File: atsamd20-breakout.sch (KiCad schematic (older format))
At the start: 37 parts, among them J1 SWD, J2 Left, J3 Right, Q1 BC847BS, SW1 SW_Push, U1 ATSAMD20E18A-A, Y1 32.768kHz, Y2 8MHz

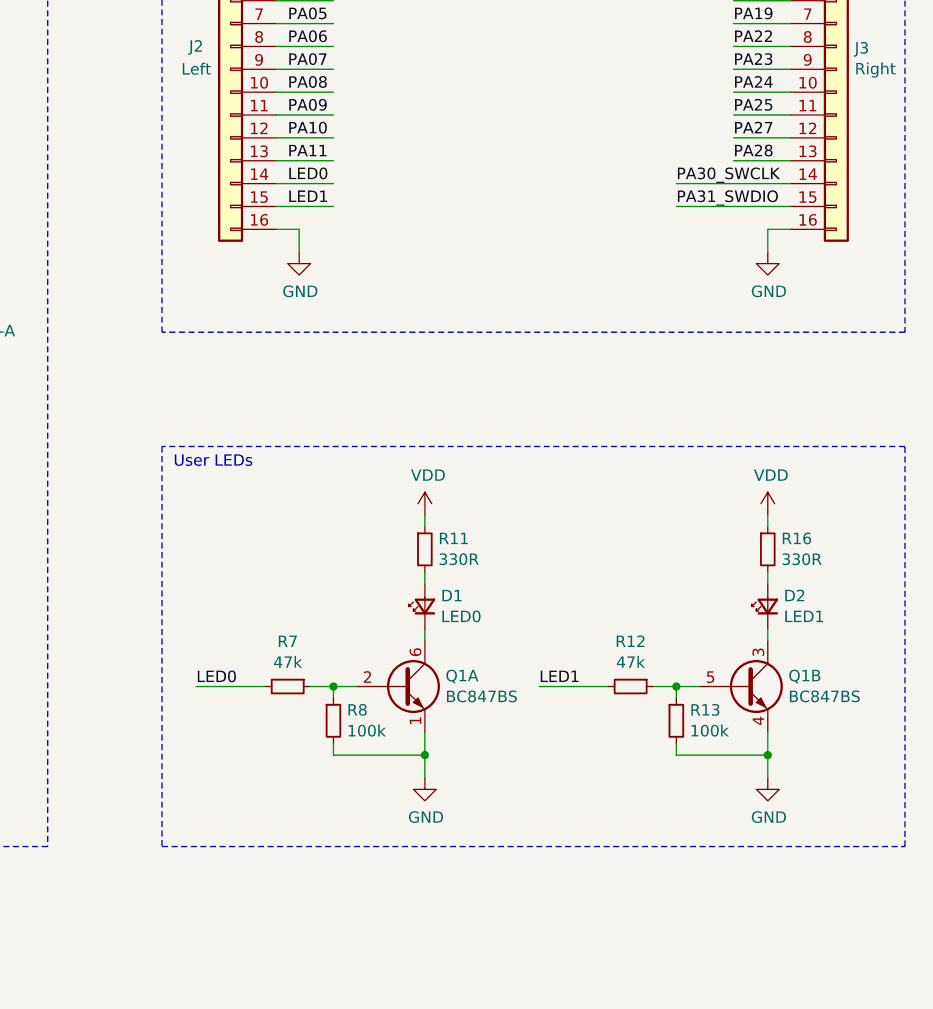
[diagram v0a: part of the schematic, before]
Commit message: Replaced LED1 pin with RESET, removed LED1 circuit
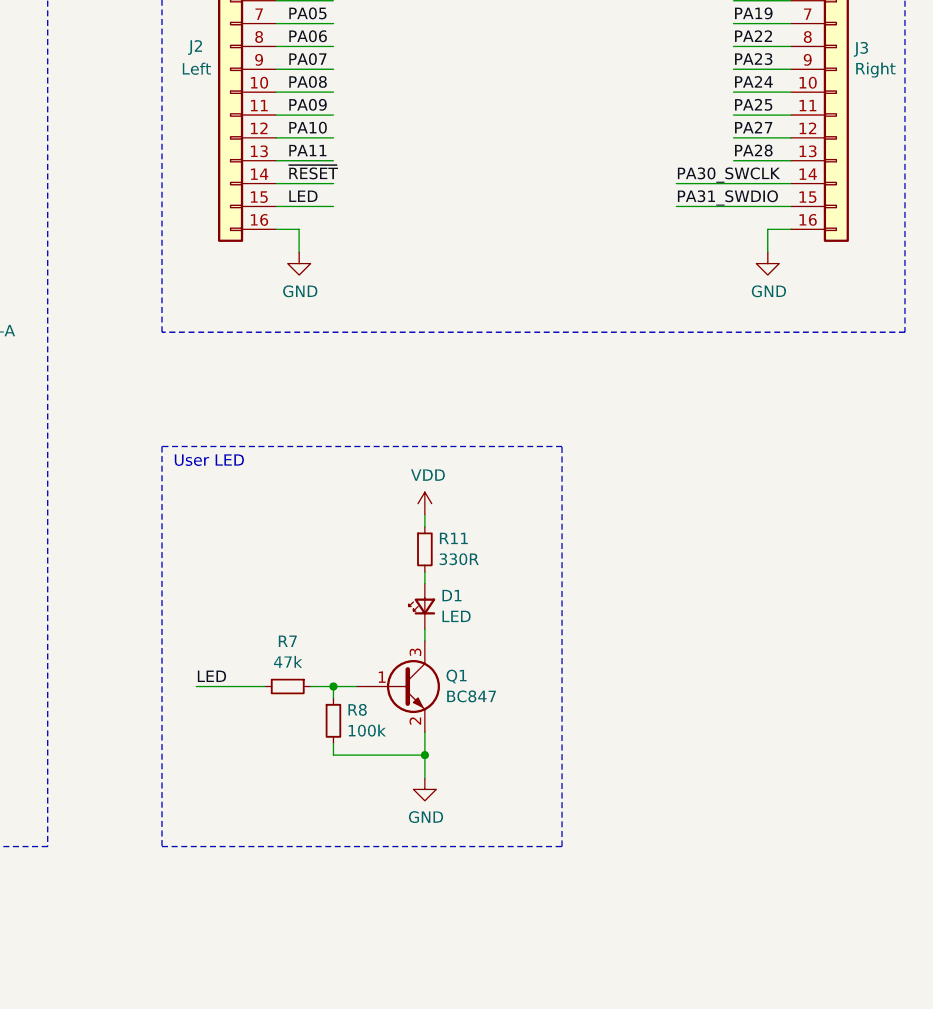
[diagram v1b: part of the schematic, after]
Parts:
- removed D2: LED1, LED_SMD:LED_0805_2012Metric, symbol Device:LED_Small
- removed Q1: BC847BS, Package_TO_SOT_SMD:SOT-363_SC-70-6, symbol Transistor_BJT:BC847BS
- removed R12: 47k, Resistor_SMD:R_0603_1608Metric, symbol Device:R_Small
- removed R13: 100k, Resistor_SMD:R_0603_1608Metric, symbol Device:R_Small
- removed R16: 330R, Resistor_SMD:R_0603_1608Metric, symbol Device:R_Small
- added Q1: BC847, Package_TO_SOT_SMD:SOT-23, symbol Transistor_BJT:BC847
- D1: value LED0 -> LED
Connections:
- net labels added: LED
- net labels removed: LED0, LED1
- wire segments 156 -> 145
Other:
- note added: "User LED"
- note removed: "User LEDs"
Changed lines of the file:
@@
 Wire Wire Line
 	9750 2950 10250 2950
-Text Label 8050 2850 0    50   ~ 0
-LED0
 Text Label 8050 2950 0    50   ~ 0
-LED1
+LED
 $Comp
 L Device:R_Small R9
@@
 Board I/O headers
 $Comp
-L Transistor_BJT:BC847BS Q1
-U 1 1 5F4F8DAD
-P 8550 5050
-F 0 "Q1" H 8740 5096 50  0000 L CNN
-F 1 "BC847BS" H 8740 5005 50  0000 L CNN
-F 2 "Package_TO_SOT_SMD:SOT-363_SC-70-6" H 8750 5150 50  0001 C CNN
-F 3 "https://assets.nexperia.com/documents/data-sheet/BC847BS.pdf" H 8550 5050 50  0001 C CNN
-	1    8550 5050
-	1    0    0    -1
-$EndComp
-$Comp
-L Transistor_BJT:BC847BS Q1
-U 2 1 5F4F9E18
-P 10050 5050
-F 0 "Q1" H 10240 5096 50  0000 L CNN
-F 1 "BC847BS" H 10240 5005 50  0000 L CNN
-F 2 "Package_TO_SOT_SMD:SOT-363_SC-70-6" H 10250 5150 50  0001 C CNN
-F 3 "https://assets.nexperia.com/documents/data-sheet/BC847BS.pdf" H 10050 5050 50  0001 C CNN
-	2    10050 5050
-	1    0    0    -1
-$EndComp
-$Comp
 L Device:LED_Small D1
 U 1 1 5F517E2A
 P 8650 4700
 F 0 "D1" V 8696 4630 50  0000 R CNN
-F 1 "LED0" V 8605 4630 50  0000 R CNN
+F 1 "LED" V 8605 4630 50  0000 R CNN
 F 2 "LED_SMD:LED_0805_2012Metric" V 8650 4700 50  0001 C CNN
 F 3 "~" V 8650 4700 50  0001 C CNN
 	1    8650 4700
-	0    -1   -1   0
-$EndComp
-$Comp
-L Device:LED_Small D2
-U 1 1 5F518B36
-P 10150 4700
-F 0 "D2" V 10196 4630 50  0000 R CNN
-F 1 "LED1" V 10105 4630 50  0000 R CNN
-F 2 "LED_SMD:LED_0805_2012Metric" V 10150 4700 50  0001 C CNN
-F 3 "~" V 10150 4700 50  0001 C CNN
-	1    10150 4700
 	0    -1   -1   0
 $EndComp
@@
 $EndComp
 $Comp
-L Device:R_Small R16
-U 1 1 5F519929
-P 10150 4450
-F 0 "R16" H 10209 4496 50  0000 L CNN
-F 1 "330R" H 10209 4405 50  0000 L CNN
-F 2 "Resistor_SMD:R_0603_1608Metric" H 10150 4450 50  0001 C CNN
-F 3 "~" H 10150 4450 50  0001 C CNN
-	1    10150 4450
-	1    0    0    -1
-$EndComp
-$Comp
 L Device:R_Small R8
 U 1 1 5F519CFF
@@
 $EndComp
 $Comp
-L Device:R_Small R13
-U 1 1 5F51A312
-P 9750 5200
-F 0 "R13" H 9809 5246 50  0000 L CNN
-F 1 "100k" H 9809 5155 50  0000 L CNN
-F 2 "Resistor_SMD:R_0603_1608Metric" H 9750 5200 50  0001 C CNN
-F 3 "~" H 9750 5200 50  0001 C CNN
-	1    9750 5200
-	1    0    0    -1
-$EndComp
-$Comp
 L Device:R_Small R7
 U 1 1 5F51A9DD
@@
 F 3 "~" H 8050 5050 50  0001 C CNN
 	1    8050 5050
-	0    1    1    0
-$EndComp
-$Comp
-L Device:R_Small R12
-U 1 1 5F51B00D
-P 9550 5050
-F 0 "R12" V 9354 5050 50  0000 C CNN
-F 1 "47k" V 9445 5050 50  0000 C CNN
-F 2 "Resistor_SMD:R_0603_1608Metric" H 9550 5050 50  0001 C CNN
-F 3 "~" H 9550 5050 50  0001 C CNN
-	1    9550 5050
 	0    1    1    0
 $EndComp
@@
 	8250 5050 8350 5050
 Wire Wire Line
-	9650 5050 9750 5050
-Wire Wire Line
-	9750 5050 9750 5100
-Connection ~ 9750 5050
-Wire Wire Line
-	9750 5050 9850 5050
-Wire Wire Line
-	9450 5050 9150 5050
-Wire Wire Line
 	7650 5050 7950 5050
 Text Label 7650 5050 0    50   ~ 0
-LED0
-Text Label 9150 5050 0    50   ~ 0
-LED1
+LED
 $Comp
 L power:GND #PWR024
@@
 	8650 5350 8650 5450
 $Comp
-L power:GND #PWR028
-U 1 1 5F56B570
-P 10150 5450
-F 0 "#PWR028" H 10150 5200 50  0001 C CNN
-F 1 "GND" H 10155 5277 50  0000 C CNN
-F 2 "" H 10150 5450 50  0001 C CNN
-F 3 "" H 10150 5450 50  0001 C CNN
-	1    10150 5450
-	1    0    0    -1
-$EndComp
-Wire Wire Line
-	10150 5250 10150 5350
-Wire Wire Line
-	9750 5300 9750 5350
-Wire Wire Line
-	9750 5350 10150 5350
-Connection ~ 10150 5350
-Wire Wire Line
-	10150 5350 10150 5450
-Wire Wire Line
-	10150 4550 10150 4600
-Wire Wire Line
-	10150 4800 10150 4850
-$Comp
 L power:VDD #PWR023
 U 1 1 5F586EB9
@@
 Wire Wire Line
 	8650 4300 8650 4350
-$Comp
-L power:VDD #PWR027
-U 1 1 5F58EA56
-P 10150 4300
-F 0 "#PWR027" H 10150 4150 50  0001 C CNN
-F 1 "VDD" H 10165 4473 50  0000 C CNN
-F 2 "" H 10150 4300 50  0001 C CNN
-F 3 "" H 10150 4300 50  0001 C CNN
-	1    10150 4300
-	1    0    0    -1
-$EndComp
-Wire Wire Line
-	10150 4300 10150 4350
 Wire Notes Line
-	7500 5750 10750 5750
+	7500 5750 9250 5750
 Wire Notes Line
-	10750 5750 10750 4000
+	9250 5750 9250 4000
 Wire Notes Line
-	10750 4000 7500 4000
+	9250 4000 7500 4000
 Wire Notes Line
 	7500 4000 7500 5750
 Text Notes 7550 4100 0    50   ~ 0
-User LEDs
+User LED
+$Comp
+L Transistor_BJT:BC847 Q1
+U 1 1 5F29391D
+P 8550 5050
+F 0 "Q1" H 8741 5096 50  0000 L CNN
+F 1 "BC847" H 8741 5005 50  0000 L CNN
+F 2 "Package_TO_SOT_SMD:SOT-23" H 8750 4975 50  0001 L CIN
+F 3 "http://www.infineon.com/dgdl/Infineon-BC847SERIES_BC848SERIES_BC849SERIES_BC850SERIES-DS-v01_01-en.pdf?fileId=db3a304314dca389011541d4630a1657" H 8550 5050 50  0001 L CNN
+	1    8550 5050
+	1    0    0    -1
+$EndComp
+Text Label 8050 2850 0    50   ~ 0
+~RESET
 $EndSCHEMATC

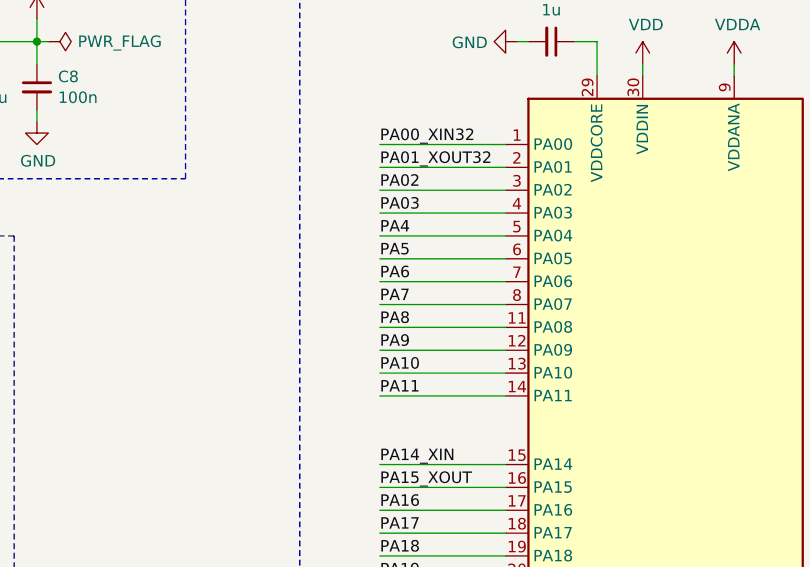
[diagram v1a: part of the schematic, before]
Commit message: Fixed net names
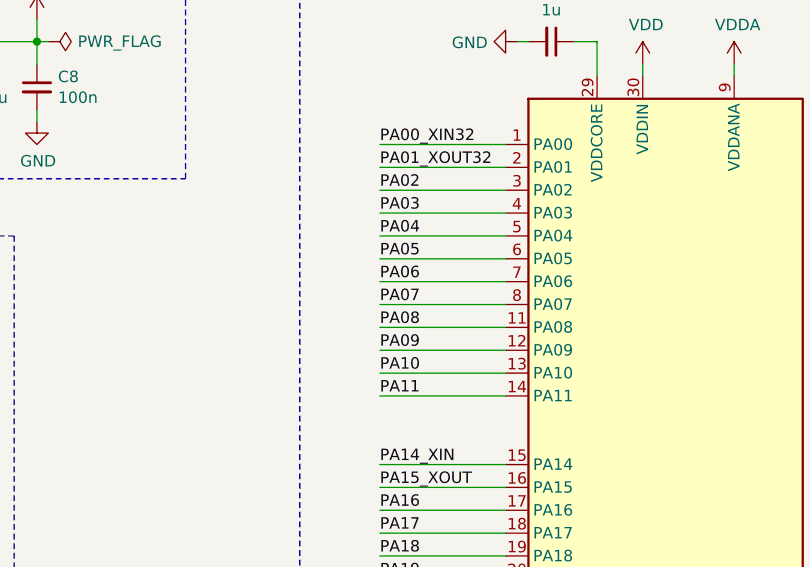
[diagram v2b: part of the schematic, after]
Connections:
- net labels removed: PA4, PA5, PA6, PA7, PA8, PA9
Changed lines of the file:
@@
 PA10
 Text Label 4350 2750 0    50   ~ 0
-PA9
+PA09
 Text Label 4350 2650 0    50   ~ 0
-PA8
+PA08
 Text Label 4350 2550 0    50   ~ 0
-PA7
+PA07
 Text Label 4350 2450 0    50   ~ 0
-PA6
+PA06
 Text Label 4350 2350 0    50   ~ 0
-PA5
+PA05
 Text Label 4350 2250 0    50   ~ 0
-PA4
+PA04
 Text Label 4350 2150 0    50   ~ 0
 PA03

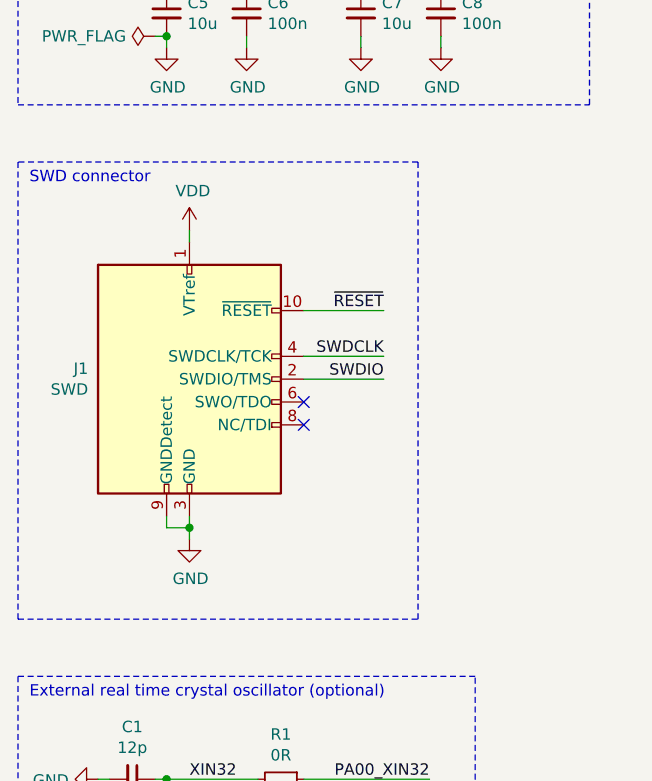
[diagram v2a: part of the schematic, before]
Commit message: Fixed SWD connector wire labels
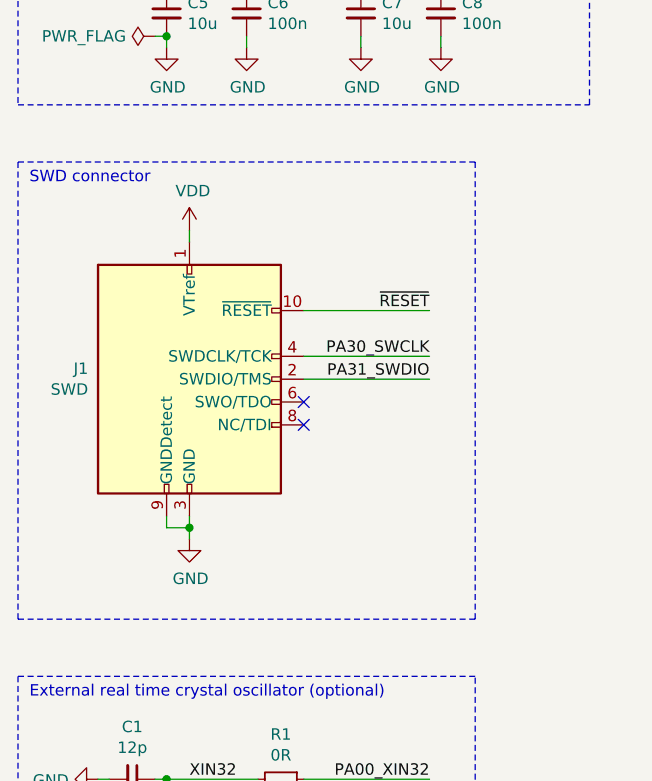
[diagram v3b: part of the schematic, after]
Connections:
- net labels removed: SWDCLK, SWDIO
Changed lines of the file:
@@
 	1750 3850 1750 3900
 Wire Wire Line
-	2250 2900 2600 2900
-Text Label 2600 2900 2    50   ~ 0
+	2250 2900 2800 2900
+Text Label 2800 2900 2    50   ~ 0
 ~RESET
 Wire Wire Line
-	2250 3100 2600 3100
+	2250 3100 2800 3100
 Wire Wire Line
-	2250 3200 2600 3200
-Text Label 2600 3100 2    50   ~ 0
-SWDCLK
-Text Label 2600 3200 2    50   ~ 0
-SWDIO
+	2250 3200 2800 3200
+Text Label 2800 3100 2    50   ~ 0
+PA30_SWCLK
+Text Label 2800 3200 2    50   ~ 0
+PA31_SWDIO
 NoConn ~ 2250 3300
 NoConn ~ 2250 3400
 Wire Notes Line
-	1000 4250 2750 4250
+	1000 4250 3000 4250
 Wire Notes Line
-	2750 4250 2750 2250
+	3000 4250 3000 2250
 Wire Notes Line
-	2750 2250 1000 2250
+	3000 2250 1000 2250
 Wire Notes Line
 	1000 2250 1000 4250

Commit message: Finished (hopefully) the layout for the Rev. A
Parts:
- SW1: value SW_Push -> Reset
- Y2: footprint Crystal:Crystal_SMD_3225-4Pin_3.2x2.5mm -> Crystal:Crystal_SMD_5032-4Pin_5.0x3.2mm
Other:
- moved on the sheet: R14, R15
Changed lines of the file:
@@
 encoding utf-8
 Sheet 1 1
-Title "ATSAMD20 Breakout Board"
-Date "2020-08-03"
+Title "ATSAMD2x Breakout Board"
+Date "2020-08-16"
 Rev "A"
-Comp "Michal Potrzebicz"
-Comment1 ""
+Comp ""
+Comment1 "Universal breakout board for ATSAMD2x MCUs"
 Comment2 ""
-Comment3 ""
+Comment3 "Michal Potrzebicz <michal@elevendroids.com>"
 Comment4 "License: CC BY-SA 4.0"
 $EndDescr
@@
 F 0 "Y2" V 1604 6794 50  0000 L CNN
 F 1 "8MHz" V 1695 6794 50  0000 L CNN
-F 2 "Crystal:Crystal_SMD_3225-4Pin_3.2x2.5mm" H 1650 6650 50  0001 C CNN
+F 2 "Crystal:Crystal_SMD_5032-4Pin_5.0x3.2mm" H 1650 6650 50  0001 C CNN
 F 3 "~" H 1650 6650 50  0001 C CNN
 	1    1650 6650
@@
 P 4200 6950
 F 0 "SW1" V 4246 6902 50  0000 R CNN
-F 1 "SW_Push" V 4155 6902 50  0000 R CNN
+F 1 "Reset" V 4155 6902 50  0000 R CNN
 F 2 "Button_Switch_SMD:SW_SPST_CK_RS282G05A3" H 4200 7150 50  0001 C CNN
 F 3 "~" H 4200 7150 50  0001 C CNN
@@
 Wire Wire Line
 	8000 2750 8250 2750
-Wire Wire Line
-	8000 2850 8250 2850
 Wire Wire Line
 	8000 2950 8250 2950
@@
 Wire Wire Line
 	10150 1550 10250 1550
+Text Label 8050 2850 0    50   ~ 0
+PA14
+Wire Wire Line
+	10250 1750 10000 1750
+Wire Wire Line
+	10250 1850 10000 1850
+Wire Wire Line
+	10250 1950 10000 1950
+Wire Wire Line
+	10250 2050 10000 2050
+Wire Wire Line
+	10250 2150 10000 2150
+Wire Wire Line
+	10250 2250 10000 2250
+Wire Wire Line
+	10250 2350 10000 2350
+Wire Wire Line
+	10250 2450 10000 2450
+Wire Wire Line
+	10250 2550 10000 2550
+Wire Wire Line
+	10250 2650 10000 2650
+Wire Wire Line
+	10250 2850 9750 2850
 Text Label 10000 1650 0    50   ~ 0
-PA14
-Wire Wire Line
-	10250 1850 10000 1850
-Wire Wire Line
-	10250 1950 10000 1950
-Wire Wire Line
-	10250 2050 10000 2050
-Wire Wire Line
-	10250 2150 10000 2150
-Wire Wire Line
-	10250 2250 10000 2250
-Wire Wire Line
-	10250 2350 10000 2350
-Wire Wire Line
-	10250 2450 10000 2450
-Wire Wire Line
-	10250 2550 10000 2550
-Wire Wire Line
-	10250 2650 10000 2650
-Wire Wire Line
-	10250 2750 10000 2750
-Wire Wire Line
-	10250 2850 9750 2850
+PA15
 Text Label 10000 1750 0    50   ~ 0
-PA15
+PA16
 Text Label 10000 1850 0    50   ~ 0
-PA16
+PA17
 Text Label 10000 1950 0    50   ~ 0
-PA17
+PA18
 Text Label 10000 2050 0    50   ~ 0
-PA18
+PA19
 Text Label 10000 2150 0    50   ~ 0
-PA19
+PA22
 Text Label 10000 2250 0    50   ~ 0
-PA22
+PA23
 Text Label 10000 2350 0    50   ~ 0
-PA23
+PA24
 Text Label 10000 2450 0    50   ~ 0
-PA24
+PA25
 Text Label 10000 2550 0    50   ~ 0
-PA25
+PA27
 Text Label 10000 2650 0    50   ~ 0
-PA27
-Text Label 10000 2750 0    50   ~ 0
 PA28
 Text Label 9750 2850 0    50   ~ 0
@@
 L Device:R_Small R14
 U 1 1 5F4BEA18
+P 8400 2850
+F 0 "R14" V 8204 2850 50  0000 C CNN
+F 1 "0R" V 8295 2850 50  0000 C CNN
+F 2 "Resistor_SMD:R_0603_1608Metric" H 8400 2850 50  0001 C CNN
+F 3 "~" H 8400 2850 50  0001 C CNN
+	1    8400 2850
+	0    -1   -1   0
+$EndComp
+$Comp
+L Device:R_Small R15
+U 1 1 5F4BF05C
 P 9850 1650
-F 0 "R14" V 9654 1650 50  0000 C CNN
-F 1 "0R" V 9745 1650 50  0000 C CNN
+F 0 "R15" V 10046 1650 50  0000 C CNN
+F 1 "0R" V 9955 1650 50  0000 C CNN
 F 2 "Resistor_SMD:R_0603_1608Metric" H 9850 1650 50  0001 C CNN
 F 3 "~" H 9850 1650 50  0001 C CNN
@@
 	0    1    1    0
 $EndComp
-$Comp
-L Device:R_Small R15
-U 1 1 5F4BF05C
-P 9850 1750
-F 0 "R15" V 10046 1750 50  0000 C CNN
-F 1 "0R" V 9955 1750 50  0000 C CNN
-F 2 "Resistor_SMD:R_0603_1608Metric" H 9850 1750 50  0001 C CNN
-F 3 "~" H 9850 1750 50  0001 C CNN
-	1    9850 1750
-	0    1    1    0
-$EndComp
-Wire Wire Line
-	9950 1750 10250 1750
 Wire Wire Line
 	9950 1650 10250 1650
 Wire Wire Line
+	8300 2850 8000 2850
+Wire Wire Line
+	8500 2850 9050 2850
+Wire Wire Line
 	9750 1650 9300 1650
-Wire Wire Line
-	9750 1750 9300 1750
+Text Label 9050 2850 2    50   ~ 0
+PA14_XIN
 Text Label 9300 1650 0    50   ~ 0
-PA14_XIN
-Text Label 9300 1750 0    50   ~ 0
 PA15_XOUT
 Wire Notes Line
@@
 	1    0    0    -1
 $EndComp
-Text Label 8050 2850 0    50   ~ 0
+Wire Wire Line
+	10250 2750 10000 2750
+Text Label 10000 2750 0    50   ~ 0
 ~RESET
 $EndSCHEMATC
